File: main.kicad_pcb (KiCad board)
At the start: 2 copper layers, 221.6 x 89.6 mm, 125 parts, among them SW1 Kailh-Choc, SW10 Kailh-Choc, SW11 Kailh-Choc, SW12 Kailh-Choc, SW13 Kailh-Choc, SW14 Kailh-Choc, SW15 Kailh-Choc, SW16 Kailh-Choc, SW17 Kailh-Choc, SW18 Kailh-Choc, SW19 Kailh-Choc, SW2 Kailh-Choc, SW20 Kailh-Choc, SW21 Kailh-Choc, SW22 Kailh-Choc, SW23 Kailh-Choc, SW24 Kailh-Choc, SW25 Kailh-Choc, SW26 Kailh-Choc, SW27 Kailh-Choc, SW28 Kailh-Choc, SW29 Kailh-Choc, SW3 Kailh-Choc, SW30 Kailh-Choc, SW31 Kailh-Choc, SW32 Kailh-Choc, SW33 Kailh-Choc, SW34 Kailh-Choc, SW4 Kailh-Choc, SW5 Kailh-Choc, SW6 Kailh-Choc, SW7 Kailh-Choc, SW8 Kailh-Choc, SW9 Kailh-Choc, U1 nice_nano, U2 nice_nano

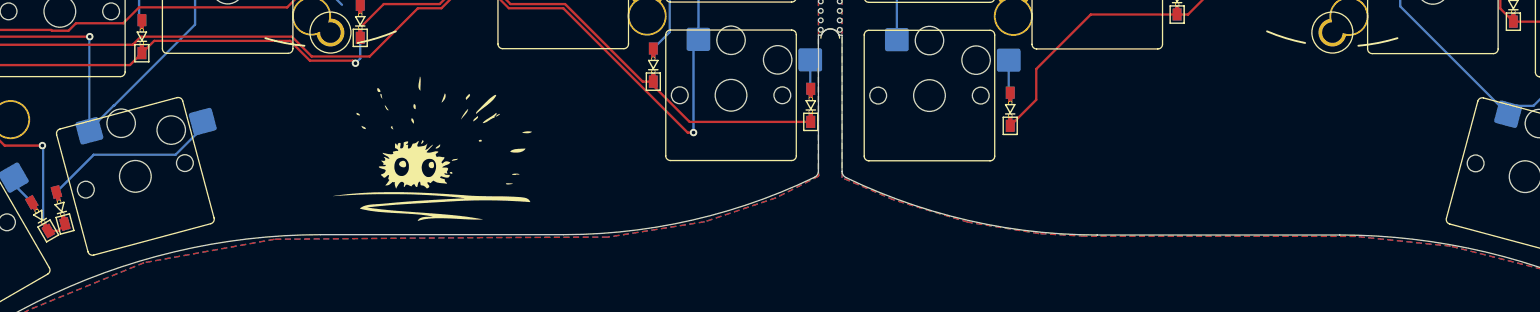
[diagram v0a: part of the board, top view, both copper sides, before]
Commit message: Add copper fill under artwork footprint
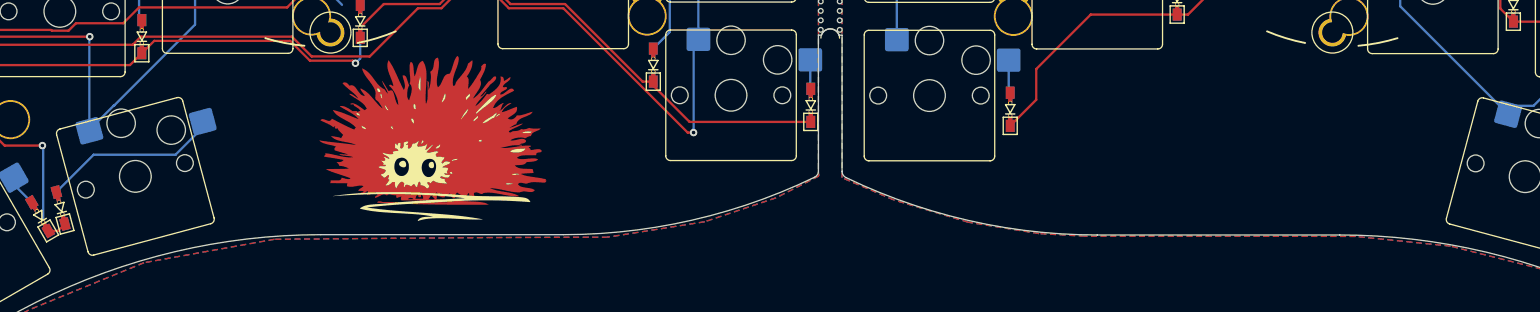
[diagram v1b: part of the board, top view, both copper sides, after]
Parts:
- added G***: LOGO, LOGO, F.Cu at (85.8, 81.8)

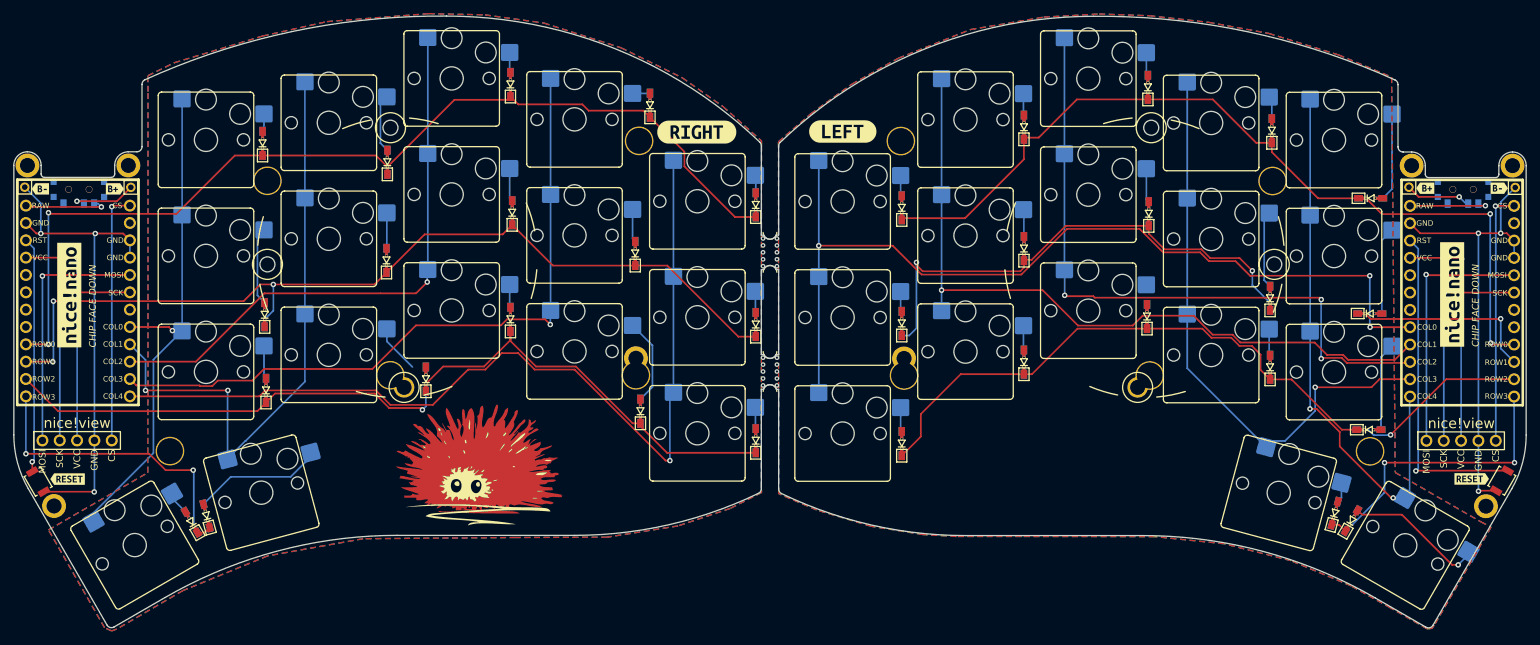
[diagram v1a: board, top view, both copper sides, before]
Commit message: Update silkscreens
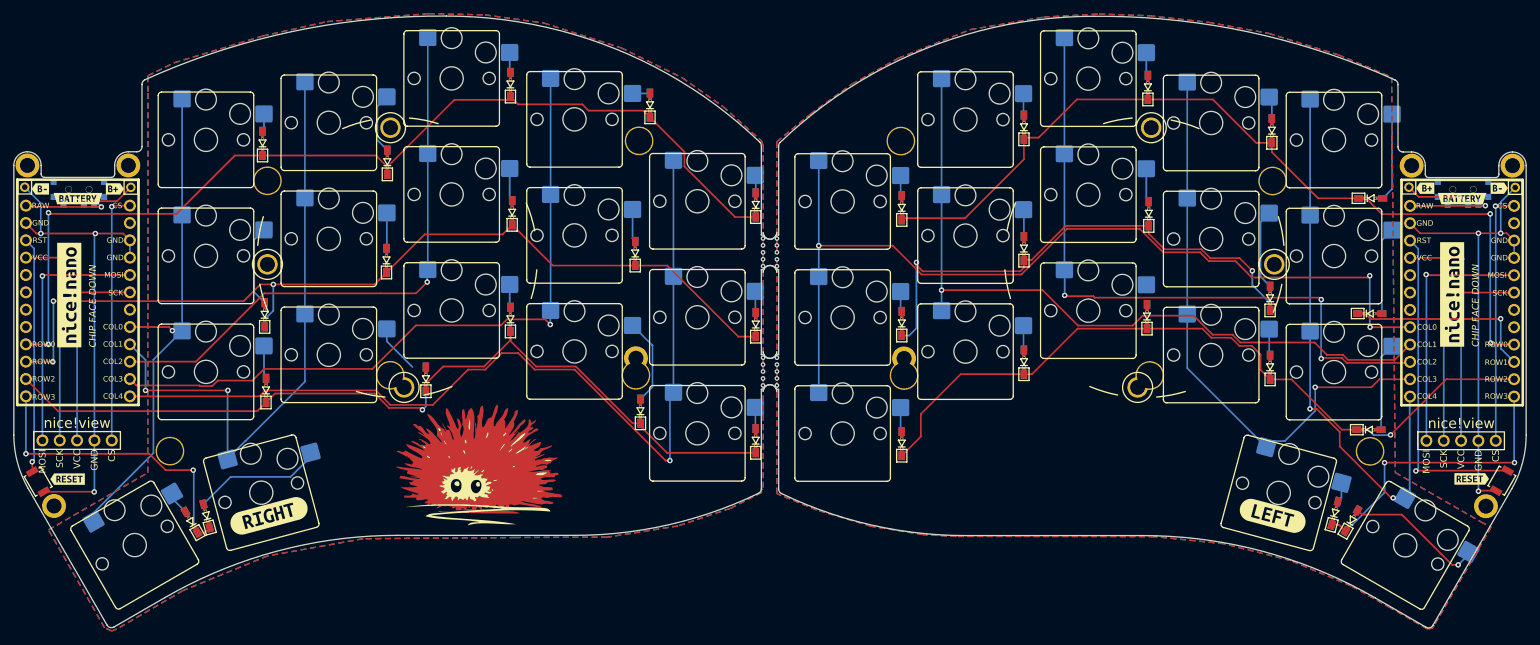
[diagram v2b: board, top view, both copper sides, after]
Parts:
- added kibuzzard-63644C3A: G***, kibuzzard-63644C3A, F.Cu at (27.0, 42.9)
- added kibuzzard-63644C57: G***, kibuzzard-63644C57, F.Cu at (229.8, 42.9)
- moved kibuzzard-636136F9 84.5 mm to (202.1, 89.4), turned to -15 degrees
- moved kibuzzard-63613726 84.2 mm to (55.0, 89.4), turned to 15 degrees
- moved kibuzzard-6361375E 36.3 mm to (54.9, 89.4), turned to -165 degrees
- moved kibuzzard-6361375E 35.0 mm to (202.1, 89.4), turned to 165 degrees

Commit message: Update silkscreen & fix DRC
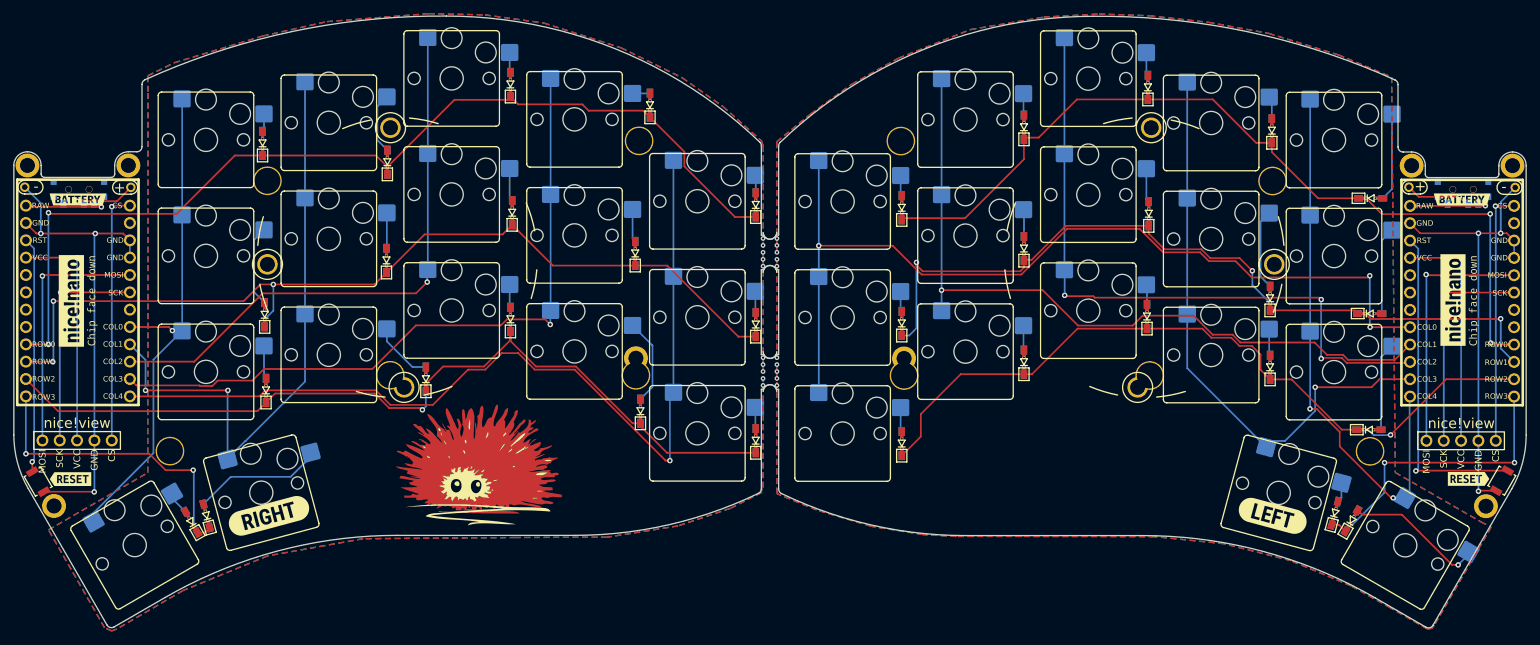
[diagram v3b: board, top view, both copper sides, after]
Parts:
- removed kibuzzard-636136F9: G***, kibuzzard-636136F9
- removed kibuzzard-63613726: G***, kibuzzard-63613726
- removed kibuzzard-6361381D (x2): G***, kibuzzard-6361381D
- removed kibuzzard-6361B5A3: G***, kibuzzard-6361B5A3
- removed kibuzzard-6361B5B5: G***, kibuzzard-6361B5B5
- removed kibuzzard-6361BA49: G***, kibuzzard-6361BA49
- removed kibuzzard-6361C84E (x2): G***, kibuzzard-6361C84E
- removed kibuzzard-6361C879: G***, kibuzzard-6361C879
- removed kibuzzard-6361C891: G***, kibuzzard-6361C891
- removed kibuzzard-6361C8A5: G***, kibuzzard-6361C8A5
- removed kibuzzard-6361C8CA: G***, kibuzzard-6361C8CA
- removed kibuzzard-6361C962: G***, kibuzzard-6361C962
- removed kibuzzard-6361C975: G***, kibuzzard-6361C975
- removed kibuzzard-6361C99D: G***, kibuzzard-6361C99D
- removed kibuzzard-6361C9A3: G***, kibuzzard-6361C9A3
- removed kibuzzard-63644C3A: G***, kibuzzard-63644C3A
- removed kibuzzard-63644C57: G***, kibuzzard-63644C57
- added kibuzzard-63658823: G***, kibuzzard-63658823, F.Cu at (55.0, 89.4)
- added kibuzzard-63658830: G***, kibuzzard-63658830, F.Cu at (202.1, 89.4)
- added kibuzzard-6365884B: G***, kibuzzard-6365884B, F.Cu at (228.5, 57.8)
- added kibuzzard-63658865: G***, kibuzzard-63658865, F.Cu at (26.0, 57.9)
- added kibuzzard-636588C8: G***, kibuzzard-636588C8, F.Cu at (231.5, 57.9)
- added kibuzzard-636588C8: G***, kibuzzard-636588C8, F.Cu at (29.1, 57.9)
- added kibuzzard-63659296: G***, kibuzzard-63659296, F.Cu at (229.8, 43.1)
- added kibuzzard-636592CC: G***, kibuzzard-636592CC, F.Cu at (27.0, 43.1)
- added kibuzzard-63659328: G***, kibuzzard-63659328, B.Cu at (87.2, 85.8)
- added kibuzzard-63659465: G***, kibuzzard-63659465, F.Cu at (25.9, 84.0)
- added kibuzzard-63659477: G***, kibuzzard-63659477, F.Cu at (230.8, 84.0)
- added kibuzzard-6365950B: G***, kibuzzard-6365950B, B.Cu at (26.9, 45.3)
- added kibuzzard-6365951E: G***, kibuzzard-6365951E, B.Cu at (230.0, 45.3)
- Bat+0, Bat+1, BatGND0, BatGND1: footprint * duckyb-collection:1pin_conn -> * duckyb-collection:1pin_Battery
- moved kibuzzard-6361375E 1.45 mm to (201.7, 90.8)
- moved kibuzzard-6361375E 1.30 mm to (55.1, 90.7)
- turned Bat+1 to 180 degrees
- turned BatGND0 to 180 degrees
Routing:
- net ROW1: track 102.1 -> 115.1 mm
- net Net-(D13-Pad2): track 0.00 -> 2.92 mm
- net Net-(D29-Pad2): track 7.15 -> 9.11 mm
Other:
- board text removed: "CHIP FACE DOWN"
